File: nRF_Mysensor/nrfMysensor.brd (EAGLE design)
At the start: 60.3 x 19.7 mm, 36 parts, among them J1 12V input, Q1 16MHz resonator, U1 ATMEGA328P-AU(R)

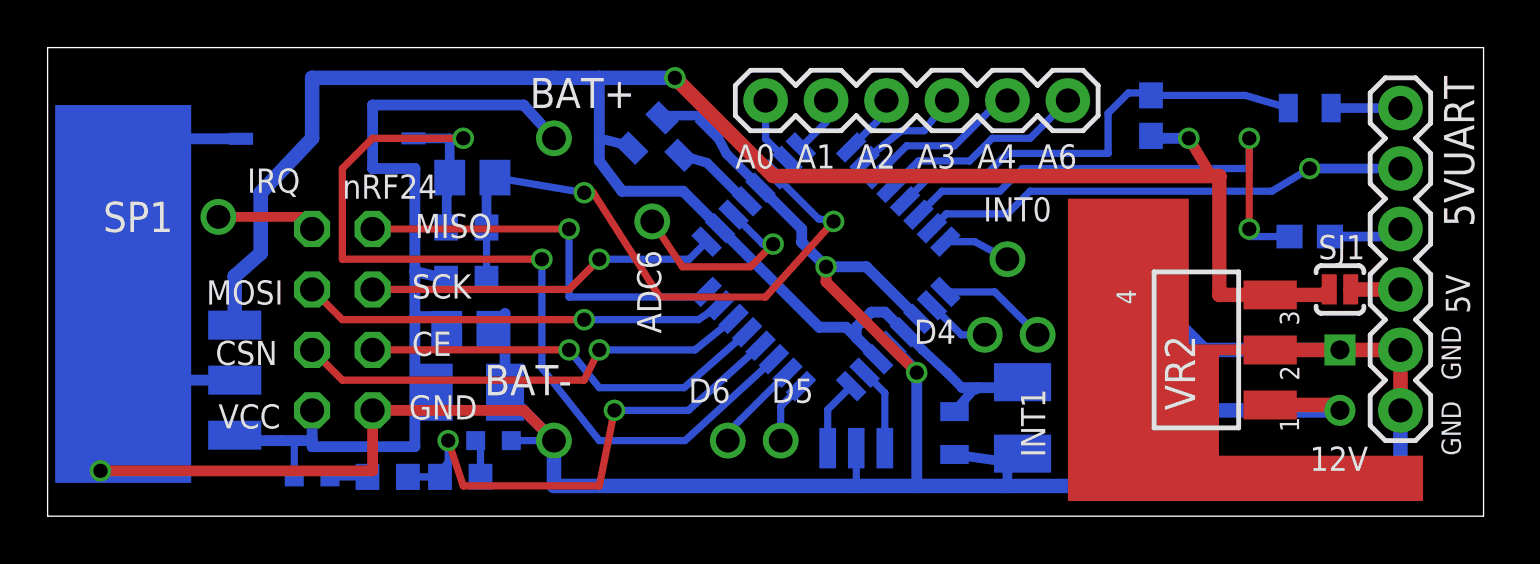
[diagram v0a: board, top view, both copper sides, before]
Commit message: nRF_MySensor board: Added resistor position for external pull up on PC0. Added spare GND and VCC solder points. Fixed R2/R3 values swapped Added more detailed build option instructions.
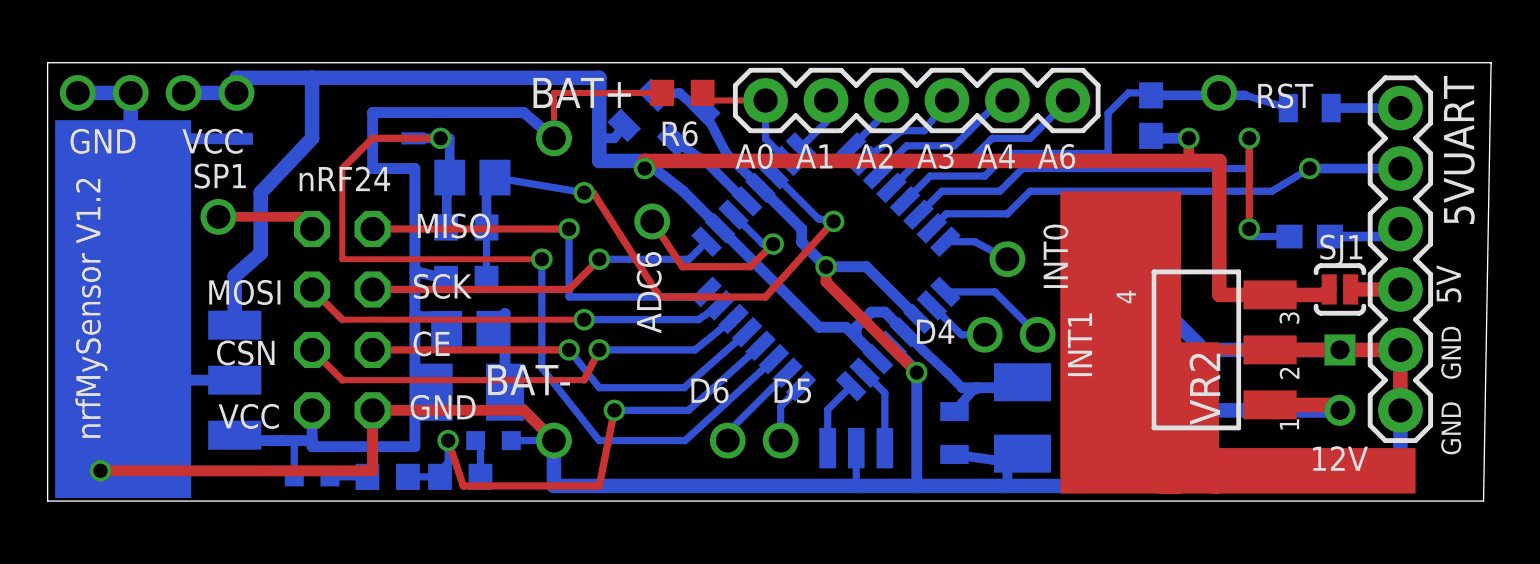
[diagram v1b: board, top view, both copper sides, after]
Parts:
- added GND, GND2, RST, VCC, VCC5: SOLDER_POINTA, 1AA_Stofer:P1-13
- added R6: 470K, rcl:R0603
- R2: value 470K -> 1M
- R3: value 1M -> 470K
- moved C4 1.00 mm to (25.2, 17.7)
- moved C5 0.71 mm to (27.2, 17.1)
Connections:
- net 5V: now also VCC.1, VCC5.1
- net A0_PC0: now also R6.2
- net GND: now also GND.1, GND2.1
- net RESET: now also RST.1
- net VCC3_3: now also R6.1
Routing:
- net VCC3_3: track 40.9 -> 46.8 mm
- net GND: track 155.4 -> 159.8 mm
- net A0_PC0: track 2.92 -> 5.88 mm
- net 5V: track 102.1 -> 99.2 mm
- net D7_PD7: track 41.1 -> 40.0 mm
- net AREF: track 3.49 -> 4.05 mm
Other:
- board size 60.3 x 19.7 mm -> 60.6 x 18.4 mm
- board text added: "nrfMySensor V1.2"
- board text removed: "IRQ"

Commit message: nrfMysensor.brd: Fixed font on version indication that was interpreted bigger by OSHPARK pcb
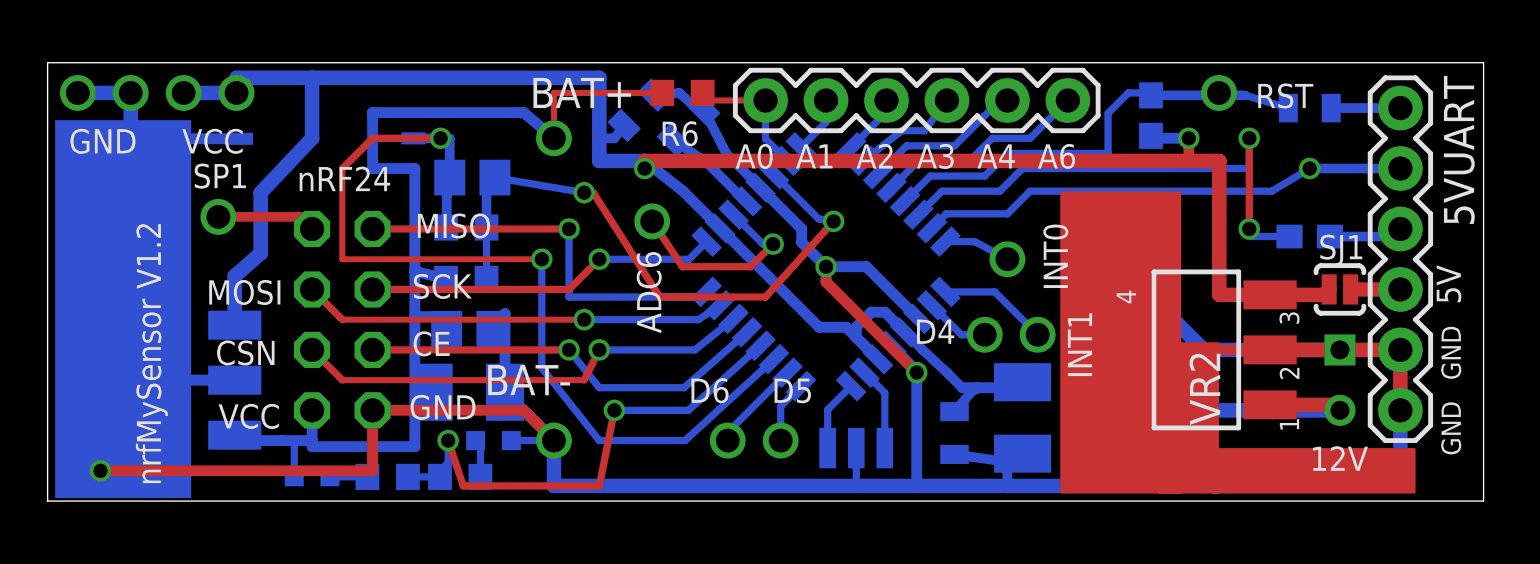
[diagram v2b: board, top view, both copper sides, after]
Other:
- board size 60.6 x 18.4 mm -> 60.3 x 18.4 mm
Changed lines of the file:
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@@
 <text x="6.985" y="9.525" size="1.016" layer="25">MOSI</text>
 <wire x1="0.3175" y1="1.27" x2="60.6425" y2="1.27" width="0" layer="20"/>
-<wire x1="60.6425" y1="1.27" x2="60.96" y2="19.685" width="0" layer="20"/>
-<wire x1="60.96" y1="19.685" x2="0.3175" y2="19.685" width="0" layer="20"/>
+<wire x1="60.6425" y1="1.27" x2="60.6425" y2="19.685" width="0" layer="20"/>
+<wire x1="60.6425" y1="19.685" x2="0.3175" y2="19.685" width="0" layer="20"/>
 <wire x1="0.3175" y1="19.685" x2="0.3175" y2="1.27" width="0" layer="20"/>
 <text x="59.69" y="3.175" size="0.8128" layer="25" rot="R90">GND</text>
@@
 <rectangle x1="46.99" y1="1.5875" x2="49.53" y2="7.9375" layer="1"/>
 <rectangle x1="49.2125" y1="1.5875" x2="57.785" y2="3.4925" layer="1"/>
-<text x="2.54" y="3.81" size="1.016" layer="25" rot="R90">nrfMySensor V1.2</text>
+<text x="5.08" y="1.905" size="1.016" layer="25" font="vector" rot="R90">nrfMySensor V1.2</text>
 </plain>
 <attributes>
